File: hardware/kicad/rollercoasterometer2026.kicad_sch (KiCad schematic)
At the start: 16 parts, among them J1 Micro_SD_Card, J102 Conn_02x07_Counter_Clockwise, J103 ZED-F9R U.FL, J104 LIS2MDL, J105 BMP595, J106 ADXL375, J4 SM03B-SRSS-TB, U101 RPiPico2, U102 ADIS16465-2BMLZ

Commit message: Updated board to four layer design
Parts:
- renumbered J1 to J101
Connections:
- net ~{CS}_MAG is gone; now on net DR_BMP: U101.26 (GP20)
- net DR_BMP: no longer U101.10 (GP7)
- no-connect marks 27 -> 29
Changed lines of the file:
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@@
 	)
 	(no_connect
+		(at 50.8 63.5)
+	)
+	(no_connect
 		(at 91.44 147.32)
 	)
@@
 	)
 	(no_connect
+		(at 53.34 66.04)
+	)
+	(no_connect
 		(at 139.7 124.46)
 	)
@@
 	(wire
 		(pts
-			(xy 85.09 76.2) (xy 101.6 76.2)
-		)
-		(stroke
-			(width 0)
-			(type default)
-		)
-	)
-	(wire
-		(pts
 			(xy 78.74 185.42) (xy 99.06 185.42)
 		)
@@
 	(wire
 		(pts
-			(xy 99.06 182.88) (xy 99.06 185.42)
+			(xy 85.09 76.2) (xy 101.6 76.2)
 		)
 		(stroke
@@
 	(wire
 		(pts
-			(xy 38.1 63.5) (xy 50.8 63.5)
+			(xy 99.06 182.88) (xy 99.06 185.42)
 		)
 		(stroke
@@
 		)
 	)
-	(label "~{CS}_MAG"
+	(label "DR_BMP"
 		(at 101.6 76.2 180)
 		(effects
@@
 		)
 	)
-	(label "DR_BMP"
-		(at 38.1 63.5 0)
-		(effects
-			(font
-				(size 1.27 1.27)
-			)
-			(justify left bottom)
-		)
-	)
 	(label "~{RST}_IMU"
 		(at 149.86 129.54 180)
@@
 		(in_pos_files yes)
 		(dnp no)
-		(fields_autoplaced yes)
 		(property "Reference" "U101"
-			(at 59.69 29.21 0)
-			(hide yes)
+			(at 67.818 35.052 0)
 			(show_name no)
 			(do_not_autoplace no)
@@
 		(property "Value" "RPiPico2"
 			(at 113.03 128.27 0)
-			(hide yes)
 			(show_name no)
 			(do_not_autoplace no)
@@
 		)
 		(pin "11"
+			(alternate "NC")
 		)
 		(pin "7"
 		)
 		(pin "10"
+			(alternate "NC")
 		)
 		(pin "5"
@@
 		)
 		(pin "1"
+			(alternate "NC")
 		)
 		(pin "8"
@@
 		(dnp no)
 		(fields_autoplaced yes)
-		(property "Reference" "J1"
+		(property "Reference" "J101"
 			(at 163.195 64.77 0)
 			(show_name no)
@@
 			(project ""
 				(path "/94683f5c-9cd9-448e-be96-9792537b5cb8"
-					(reference "J1")
+					(reference "J101")
 					(unit 1)
 				)

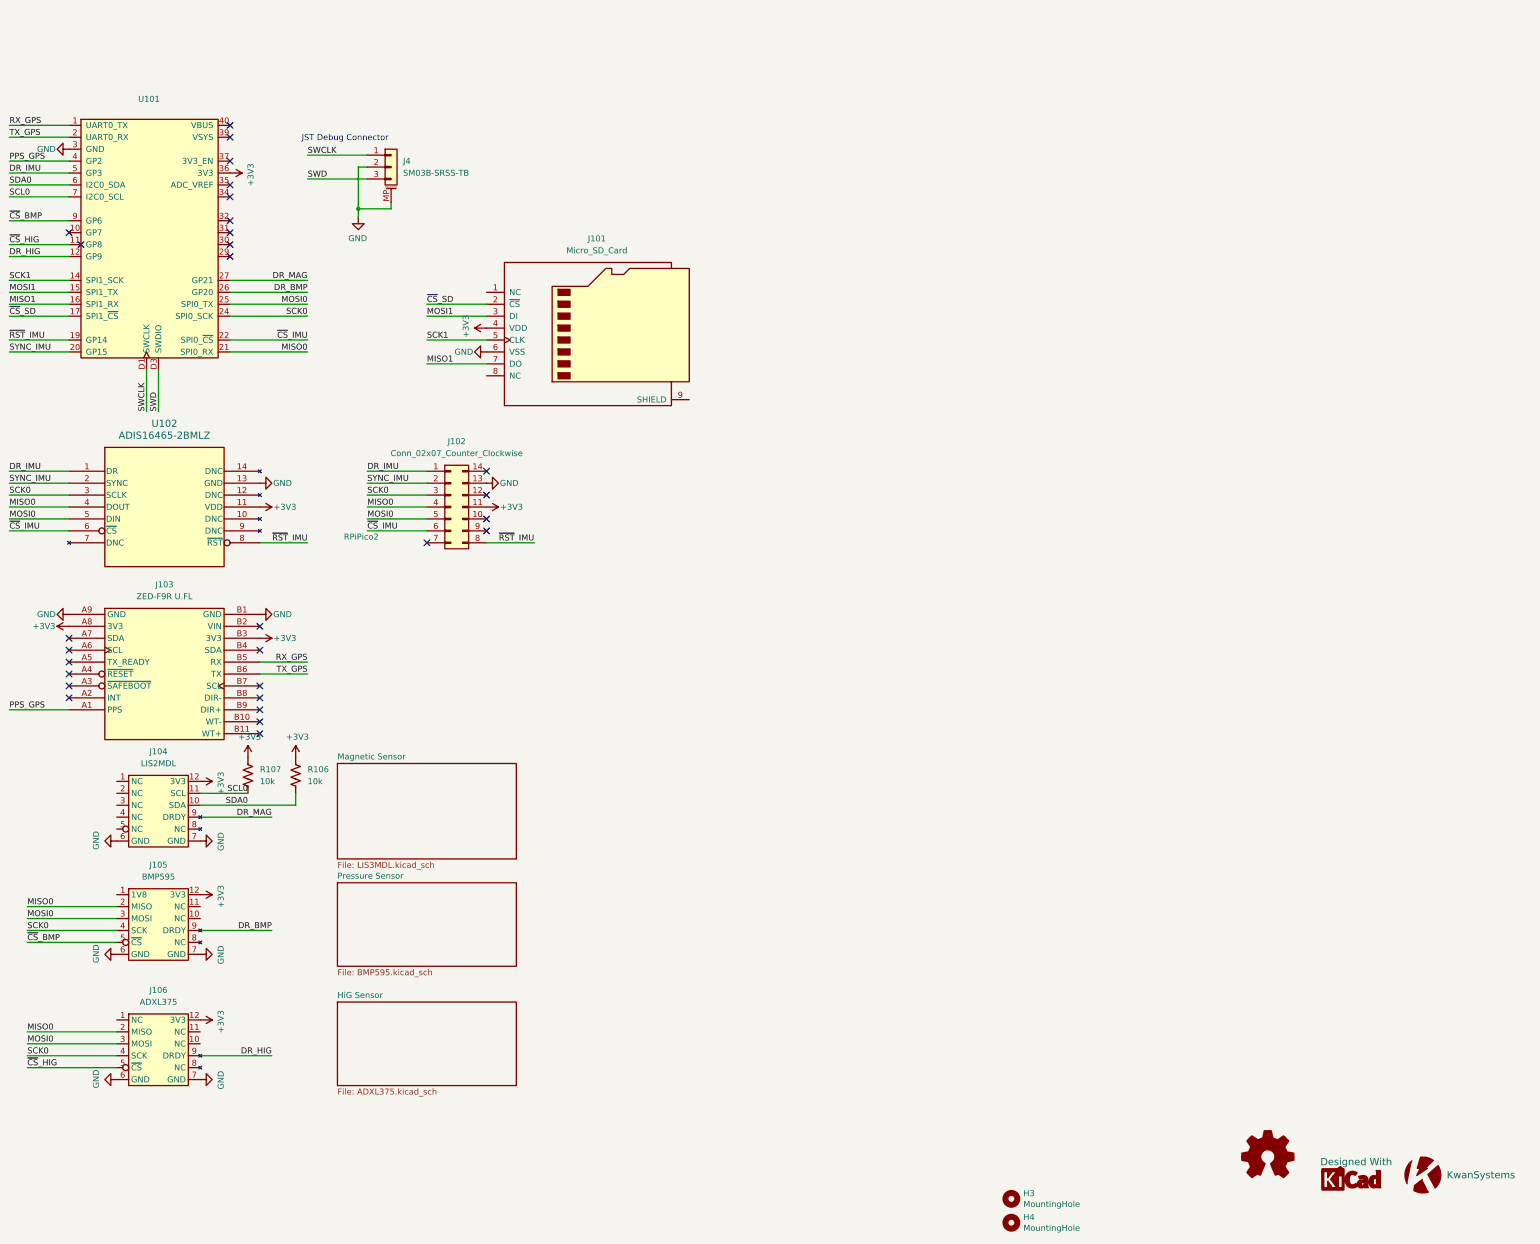
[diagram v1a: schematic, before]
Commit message: Moved sensors from stamp to direct placement
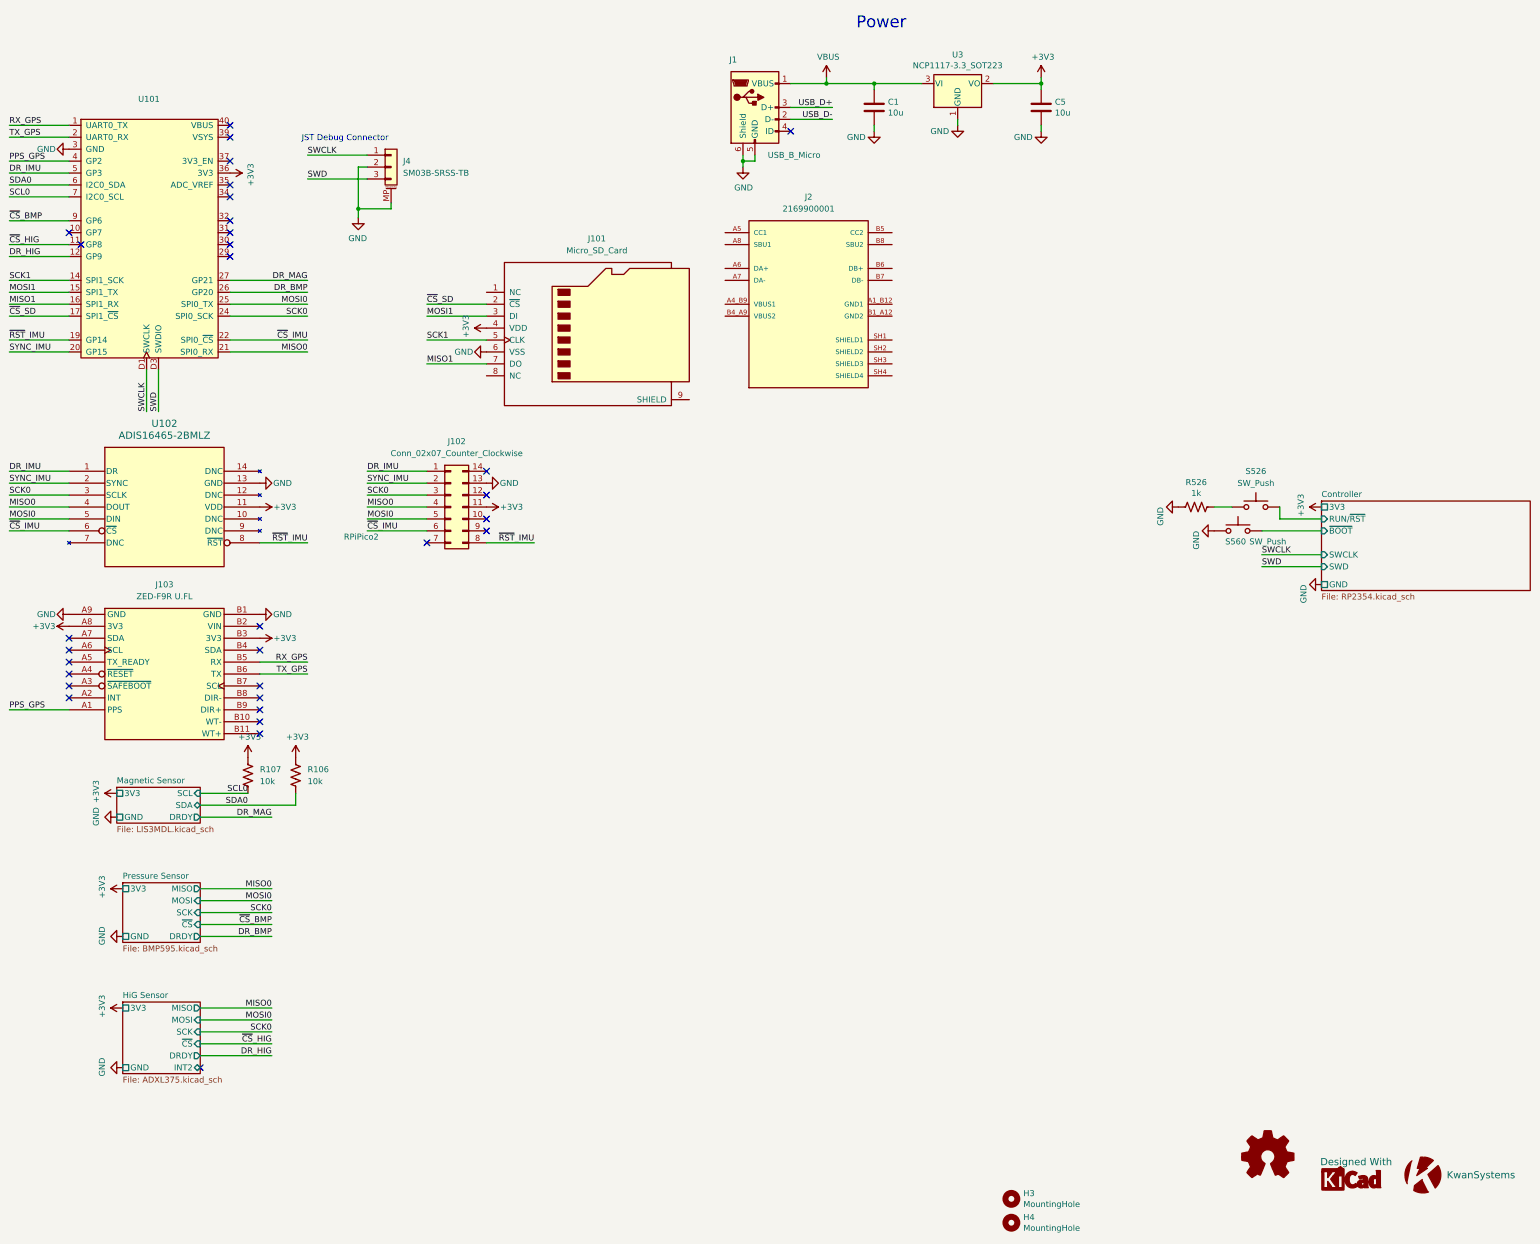
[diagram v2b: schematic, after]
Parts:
- removed J104: LIS2MDL, footprints:StampPad, symbol rollercoasterometer2026:STAMP
- removed J105: BMP595, footprints:StampPad, symbol rollercoasterometer2026:STAMP
- removed J106: ADXL375, footprints:StampPad, symbol rollercoasterometer2026:STAMP
- added C1, C5: 10u, Capacitor_SMD:C_0805_2012Metric, symbol Device:C
- added J1: USB_B_Micro, Connector_USB:USB_Micro-B_Amphenol_10103594-0001LF_Horizontal, symbol Connector:USB_B_Micro
- added J2: 2169900001, footprints:MOLEX_2169900001, symbol rollercoasterometer2026:2169900001
- added R526: 1k, Resistor_SMD:R_0402_1005Metric, symbol Device:R_US
- added S526, S560: SW_Push, Button_Switch_SMD:SW_Push_1P1T_NO_Vertical_Wuerth_434133025816, symbol Switch:SW_Push
- added U3: NCP1117-3.3_SOT223, Package_TO_SOT_SMD:SOT-223-3_TabPin2, symbol Regulator_Linear:NCP1117-3.3_SOT223
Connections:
- net +3V3: now also C5.1, U3.2 (VO)
- net GND: now also C1.2, C5.2, J1.5 (GND), J1.6 (Shield), R526.2, S560.1, U3.1 (GND)
- new net: R526.1, S526.1
- new net Controller/RUN/~{RST}: S526.2
- new net Controller/~{BOOT}: S560.2
- new net USB_D+: J1.3 (D+)
- new net USB_D-: J1.2 (D-)
- new net VBUS: C1.1, J1.1 (VBUS), U3.3 (VI)
- no-connect marks 29 -> 31
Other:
- added sheet Controller (RP2354.kicad_sch)
- sheet HiG Sensor ports: added 3V3, DRDY, GND, INT2, MISO, MOSI, SCK, ~{CS}; removed none
- sheet Magnetic Sensor ports: added 3V3, DRDY, GND, SCL, SDA; removed none
- sheet Pressure Sensor ports: added 3V3, DRDY, GND, MISO, MOSI, SCK, ~{CS}; removed none
- note added: "Power"

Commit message: Import rp2354 module
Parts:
- removed J1: USB_B_Micro, Connector_USB:USB_Micro-B_Amphenol_10103594-0001LF_Horizontal, symbol Connector:USB_B_Micro
- removed U101: RPiPico2, footprints:RaspberryPi_Pico_Original_SMD, symbol rollercoasterometer2026:RaspberryPiPico2
- added H101, H102: MountingHole, MountingHole:MountingHole_2.7mm_M2.5, symbol Mechanical:MountingHole
- added R101, R102: 5.1k, Resistor_SMD:R_0402_1005Metric, symbol Device:R_US
- R106, R107: footprint Resistor_SMD:R_0603_1608Metric -> Resistor_SMD:R_0402_1005Metric
- S526: footprint Button_Switch_SMD:SW_Push_1P1T_NO_Vertical_Wuerth_434133025816 -> Button_Switch_SMD:SW_SPST_B3U-1000P; symbol Switch:SW_Push -> Switch:SW_SPST
- S560: symbol Switch:SW_Push -> Switch:SW_SPST
- renumbered C5 to C102, C1 to C103, H3 to H103, H4 to H104, J2 to J104, J4 to J105, U3 to U101
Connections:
- net GND: now also J104.A1_B12 (GND1), J104.B1_A12 (GND2), R101.2, R102.1
- net USB_D+: now also J104.A6 (DA+), J104.B6 (DB+)
- net USB_D-: now also J104.A7 (DA-), J104.B7 (DB-)
- net VBUS: now also J104.A4_B9 (VBUS1), J104.B4_A9 (VBUS2)
- net CC1: now reaches J104.A5 (CC1)
- net CC1: now also R101.1
- net CC2: now reaches J104.B5 (CC2)
- net CC2: now also R102.2
- net Controller/RUN/~{RST} renamed ~{RESET}
- net Controller/~{BOOT} renamed ~{BOOT}
- no-connect marks 31 -> 34
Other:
- sheet Controller ports: added GPIO0, GPIO1, GPIO10, GPIO11, GPIO12, GPIO13, GPIO14, GPIO15, GPIO16, GPIO17, GPIO18, GPIO19, GPIO2, GPIO20, GPIO21, GPIO22, GPIO23, GPIO24, GPIO25, GPIO26_ADC0, GPIO27_ADC1, GPIO28_ADC2, GPIO29_ADC3, GPIO3, GPIO4, GPIO5, GPIO6, GPIO7, GPIO8, GPIO9, USB_D+, USB_D-; removed none
- moved on the sheet: H104, J101, J104, R526
